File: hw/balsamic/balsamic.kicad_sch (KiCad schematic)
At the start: 54 parts, among them J1 AXT524124, J3 USB_B_Mini, SW1 SW_Push, U1 ISP1807-LR-RS, U2 BMI160, U3 MAX77651BEWVA+T

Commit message: Added symbols and 3D models. Edited schematic
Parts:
- removed C45: 100nF, Capacitor_SMD:C_0201_0603Metric, symbol Device:C_Small
- removed D1: LED, LED_SMD:LED_0402_1005Metric, symbol Device:LED
- removed R20: NO_STUFF, Resistor_SMD:R_0201_0603Metric, symbol Device:R_Small
- removed R33: 200, Resistor_SMD:R_0201_0603Metric, symbol Device:R_Small
- removed SW1: SW_Push, Resistor_SMD:R_0603_1608Metric, symbol Switch:SW_Push
- removed TP17, TP18, TP19, TP20: TestPoint, custom_testpoints:TestPoint_THTPad_1.0x1.0mm_Drill0.5mm, symbol Connector:TestPoint
- removed U2: BMI160, Package_LGA:Bosch_LGA-14_3x2.5mm_P0.5mm, symbol Sensor_Motion:BMI160
- added C13: 10uF, Capacitor_SMD:C_0201_0603Metric, symbol Device:C_Small
- added C6: 100nF, Capacitor_SMD:C_0201_0603Metric, symbol Device:C_Small
- added R1: NO_STUFF, Resistor_SMD:R_0201_0603Metric, symbol Device:R_Small
- added R2: 10K, Resistor_SMD:R_0201_0603Metric, symbol Device:R_Small
- added TP1, TP11, TP2, TP3, TP4: TestPoint, custom_testpoints:TestPoint_Pad_D0.5mm, symbol Connector:TestPoint
- added U1: BMI270, footprints:XDCR_BMI270, symbol BMI270:BMI270
- renumbered C47 to C10, C7 to C11, C5 to C12, C48 to C14, C49 to C15, C50 to C16, C6 to C17, C12 to C18, C9 to C3, C3 to C4, C10 to C5, C4 to C7, C11 to C9, D2 to D1, J3 to J1, J1 to J2, L2 to L1, R1 to R3, R34 to R4, R2 to R5, R15 to R7, R16 to R8, TP7 to TP10, TP2 to TP12, TP15 to TP13, TP16 to TP14, TP8 to TP15, TP9 to TP16, TP10 to TP17, TP11 to TP18, TP12 to TP19, TP13 to TP20, TP14 to TP21, TP1 to TP5, TP3 to TP6, TP4 to TP7, TP5 to TP8, TP6 to TP9, U3 to U2, U1 to U3
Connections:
- net PMU_SDA is gone; now on net DVP_SDA: U2.A3 (SDA), U3.57 (P1_00_TRACEDATA0)
- net +1V8: now also R1.2; no longer C12.1, U2.B6 (IN_LDO), U2.C4 (VIO)
- net Button: now also TP1.1
- net DVP_SDA: no longer U3.3 (P0_12_TRACEDATA1)
- net GND: now also C13.1, C6.2, TP3.1, U1.6 (GNDIO), U1.7 (GND)
- net IMU_CLK: now also U1.13 (SCX)
- net IMU_CS: now also U1.12 (CSB)
- net IMU_INT1: now also U1.4 (INT1)
- net IMU_INT2: now also TP4.1, U1.9 (INT2)
- net IMU_MISO: now also U1.1 (SDO)
- net IMU_MOSI: now also U1.14 (SDX)
- net PMU_VSYS: now also R2.1
- net VDD: now also U2.B6 (IN_LDO), C13.2
- net VDDA: now also C12.1, U2.C4 (VIO)
- net nRF_LED1: now also TP2.1
- net nRF_P1_06: now also C6.1, R1.1, U1.5 (VDDIO), U1.8 (VDD)
- net nRF_UART_TX: now also U3.37 (P0_15); no longer U3.36 (P0_05_AIN3)
- net nRF_UART_RX: now reaches U3.39 (P0_27)
- net nRF_UART_RX: now also TP11.1
- net at U2.A2 (NEN): now also R2.2
- net DVP_D4: no longer names the net of J2.18
- net DVP_D5: no longer names the net of J2.20
- net DVP_D6: no longer names the net of J2.22
- net DVP_D7: no longer names the net of J2.24
- net PMU_NIRQ: no longer names the net of U3.62 (P1_07)
- net PMU_NIRQ: no longer U2.C2 (NIRQ)
- net PMU_VSBB2: no longer names the net of U2.E6 (SBB2)
- net nRF_P0_02: no longer names the net of U3.40 (P0_02_AIN0)
- net nRF_P0_03: no longer names the net of U3.38 (P0_03_AIN1)
- net nRF_P0_05: no longer names the net of U3.35 (P0_04_AIN2)
- net nRF_P0_30: no longer names the net of U3.44 (P0_30_AIN6)
- net nRF_P0_31: no longer names the net of U3.42 (P0_31_AIN7)
- net nRF_P1_01: no longer names the net of U3.64 (P1_01)
- net nRF_P1_04: no longer names the net of U3.63 (P1_04)
- net nRF_P1_10: no longer names the net of U3.60 (P1_10)
- net nRF_P1_11: no longer names the net of U3.61 (P1_11)
- net nRF_P1_12: no longer names the net of U3.59 (P1_12)
- net nRF_P1_13: no longer names the net of U3.53 (P1_13)
- net nRF_P1_14: no longer names the net of U3.52 (P1_14)
- new net nRF_P0_12: U3.3 (P0_12_TRACEDATA1)
- no-connect marks 32 -> 49
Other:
- note added: "Button & LED"
- note added: "Camera IO Power"
- note added: "Connections to LED/Button Board"
- note added: "Internal pullup on nRF; trigger interrupt to wake nRF"
- note removed: "0603 size pads for button"
- note removed: "BMI270"
- note removed: "Button"
- note removed: "Connections to 2nd Board"
- note removed: "Internal Pullup on nRF; trigger interrupt to wake nRF"
- moved on the sheet: C1, C10, C14, C15, C16, C17, C18, C3, C5, C7, C8, C9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

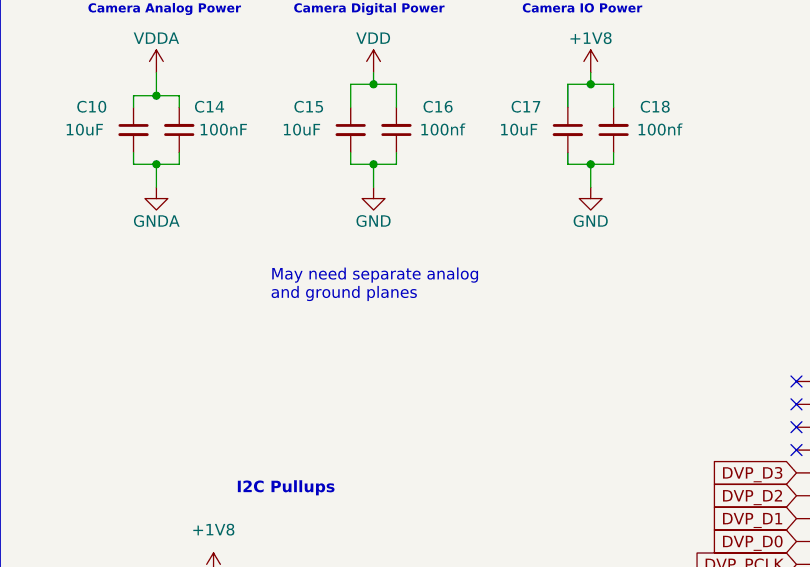
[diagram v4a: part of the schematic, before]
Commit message: Began 2 layer-routing
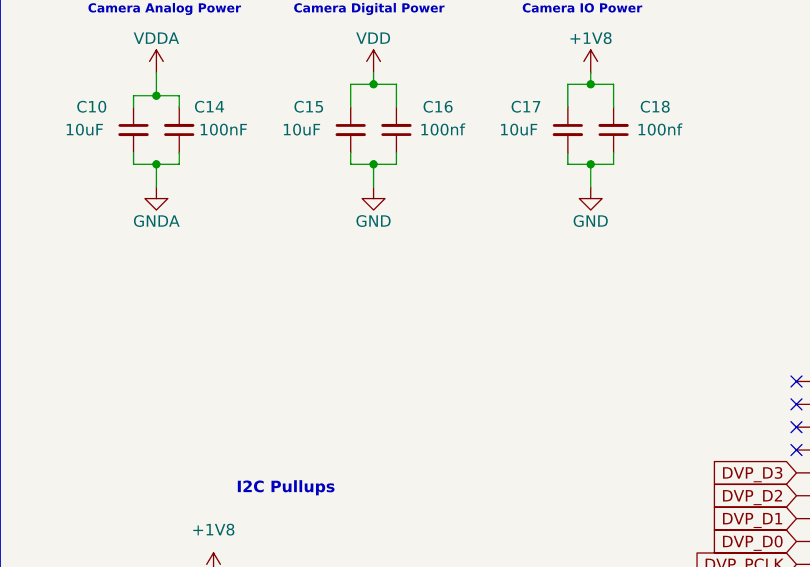
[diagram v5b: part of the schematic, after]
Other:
- note removed: "May need separate analog and ground planes"
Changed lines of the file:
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@@
-    (effects (font (size 1.27 1.27)) (justify left bottom))
-  )
-  (text "May need separate analog\nand ground planes" (at 299.72 54.61 0)
     (effects (font (size 1.27 1.27)) (justify left bottom))
   )

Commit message: Began layout of flex-pcb
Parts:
- removed J1: USB_B_Mini, Connector_USB:USB_Micro-B_GCT_USB3076-30-A, symbol Connector:USB_B_Mini
- removed TP1, TP2, TP3: TestPoint, custom_testpoints:TestPoint_Pad_D0.5mm, symbol Connector:TestPoint
- added BT2: GREPOW_Battery, footprints:balsamic_grepow_battery, symbol kendryte-power:GREPOW_Battery
- added D2: LED, LED_SMD:LED_0402_1005Metric, symbol Device:LED
- added J1: 5034800440, footprints:CON_5034800440_MOL, symbol molex-5034800440:5034800440
- added R6: 200, Resistor_SMD:R_0201_0603Metric, symbol Device:R_Small
- added SW1: SW_SPST, footprints:SW4-SMD-5.2X5.2X1.5MM, symbol Switch:SW_SPST
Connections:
- net +1V8: now also D2.2 (A)
- net BATT: now also BT2.1 (+)
- net GND: now also BT2.2 (-), J1.P1, J1.P2, SW1.2 (B)
- net VBUS_USB: now also J1.1
- net nRF_LED1: now also R6.1
- net nRF_SWDCLK: now also J1.3
- net nRF_SWDIO: now also J1.2
- net Button renamed nRF_P0_07
- net nRF_P0_07: now also SW1.1 (A)
- new net: D2.1 (K), R6.2
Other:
- note added: "Button"
- note added: "Molex Easy-On FFC/FPC Connector"
- note removed: "Button & LED"
- note removed: "Connections to LED/Button Board"
- note removed: "USB B Port"

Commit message: First full routing attempt
- Switched to using a 4 layer board on the islands.
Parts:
- removed J1: 5034800440, footprints:CON_5034800440_MOL, symbol molex-5034800440:5034800440
- removed R1: NO_STUFF, Resistor_SMD:R_0201_0603Metric, symbol Device:R_Small
- removed SW1: SW_SPST, footprints:SW4-SMD-5.2X5.2X1.5MM, symbol Switch:SW_SPST
- added J3: USB_B_Micro, Connector_USB:USB_Micro-B_GCT_USB3076-30-A, symbol Connector:USB_B_Micro
- added S1: B3U-1000P, footprints:SW_B3U-1000P, symbol B3U-1000P-Button:B3U-1000P
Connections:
- net GNDA is gone; now on net GND: C10.2, C14.1, J2.23
- net nRF_P0_07 is gone; now on net nRF_LED1: U3.33 (P0_07_TRACECLK)
- net GND: now also J3.5 (GND), J3.6 (Shield), S1.2
- net IMU_CLK: now also U3.36 (P0_05_AIN3); no longer U3.27 (P0_17)
- net IMU_CS: now also U3.38 (P0_03_AIN1); no longer U3.29 (P0_13)
- net IMU_INT1: now also U3.40 (P0_02_AIN0); no longer U3.51 (P1_15)
- net IMU_INT2: now also U3.42 (P0_31_AIN7); no longer U3.49 (P1_02)
- net IMU_MISO: now also U3.32 (P0_08); no longer U3.19 (P0_24)
- net IMU_MOSI: now also U3.34 (P0_06); no longer U3.58 (P1_03)
- net VBUS_USB: now also J3.1 (VBUS)
- net VDDA: now also C6.1, U1.5 (VDDIO), U1.8 (VDD)
- net nRF_LED1: no longer U3.32 (P0_08)
- net nRF_LED2: now also U3.35 (P0_04_AIN2); no longer U3.34 (P0_06)
- net nRF_P1_06: no longer C6.1, U1.5 (VDDIO), U1.8 (VDD), U3.50 (P1_06)
- net nRF_SWDCLK: now also J3.2 (D-)
- net nRF_SWDIO: now also J3.3 (D+)
- net nRF_P0_14: now reaches U3.5 (P0_14)
- net nRF_P0_14: now also TP11.1
- net nRF_P0_26: now reaches U3.6 (P026)
- net nRF_P0_26: now also TP10.1
- net PMU_GPIO_0: no longer names the net of U3.54 (P1_05)
- net PMU_GPIO_0: no longer U2.B1 (GPIO)
- net nRF_P0_12: no longer names the net of U3.3 (P0_12_TRACEDATA1)
- net nRF_UART_RX: no longer names the net of U3.39 (P0_27)
- net nRF_UART_RX: no longer TP11.1
- net nRF_UART_TX renamed BUTTON
- net BUTTON: now also S1.1; no longer TP10.1
- no-connect marks 49 -> 53
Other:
- note added: "Micro USB"
- note removed: "Molex Easy-On FFC/FPC Connector"

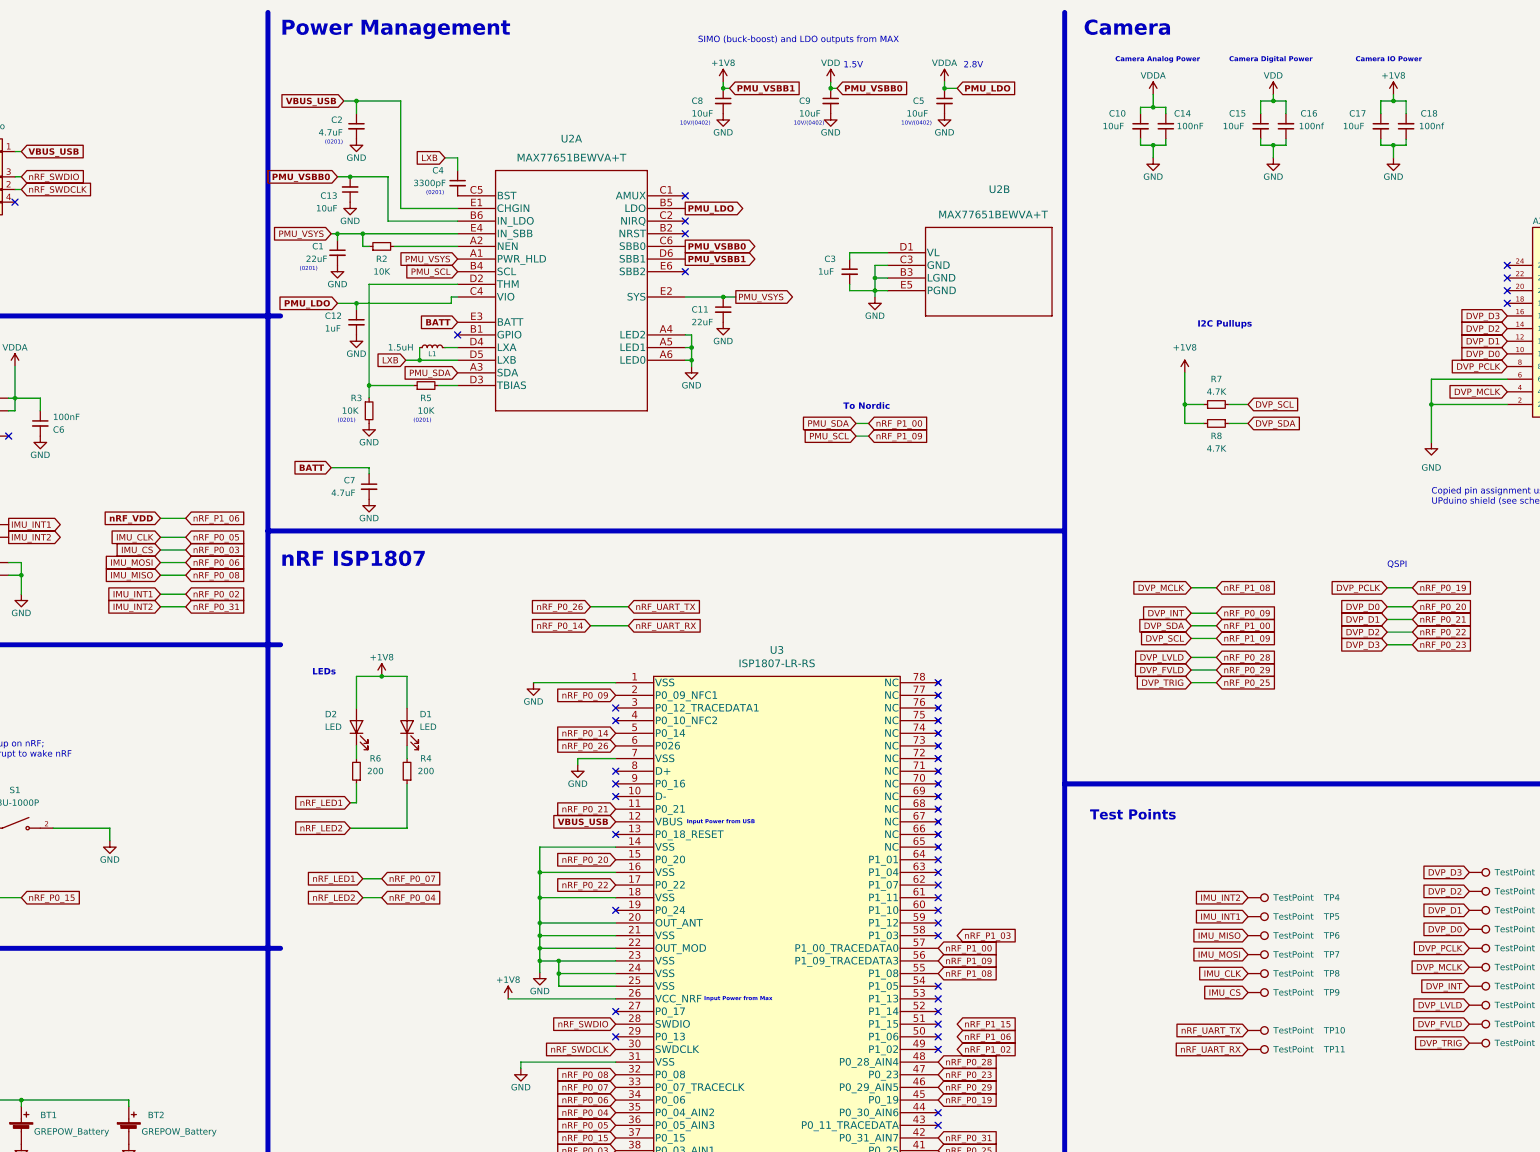
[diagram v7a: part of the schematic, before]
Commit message: incorporated Malik's board feedback
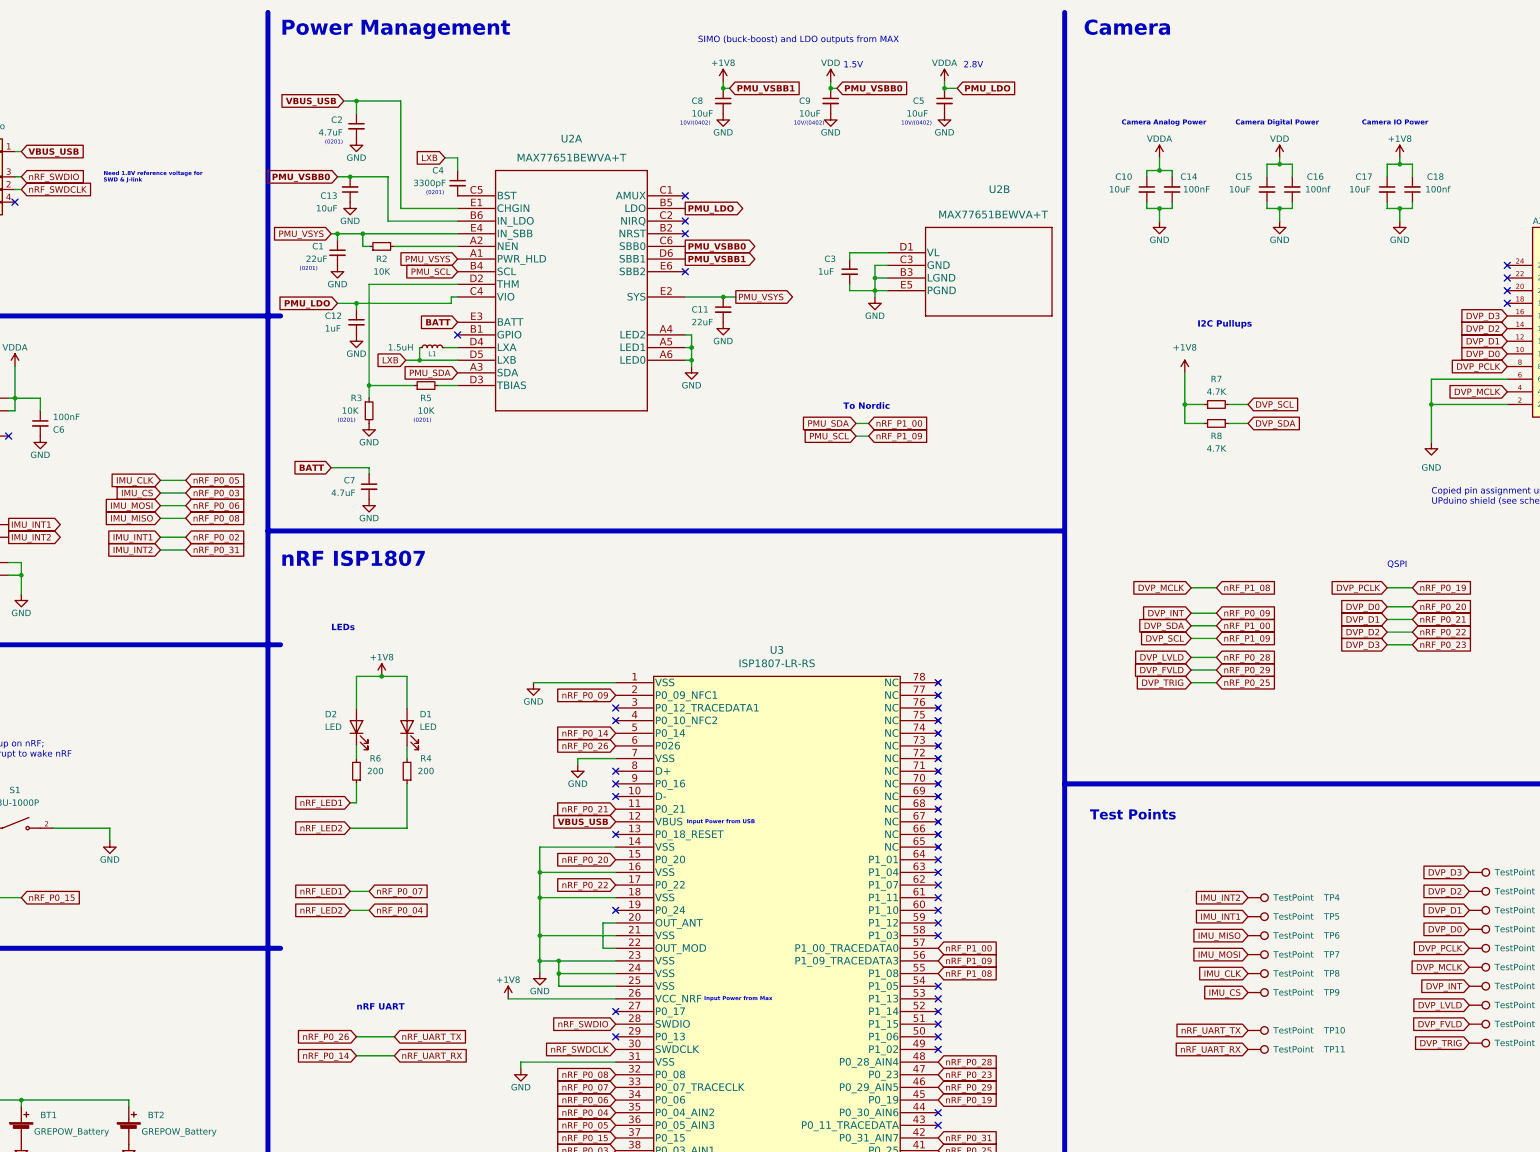
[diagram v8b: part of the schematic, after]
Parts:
- L1: footprint Inductor_SMD:L_0603_1608Metric -> Inductor_SMD:L_0805_2012Metric
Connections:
- net GND: no longer U3.20 (OUT_ANT), U3.22 (OUT_MOD)
- new net: U3.20 (OUT_ANT), U3.22 (OUT_MOD)
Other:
- note added: "Need 1.8V reference voltage for SWD & J-link"
- note added: "nRF UART"
- moved on the sheet: C10, C14, C15, C16, C17, C18
